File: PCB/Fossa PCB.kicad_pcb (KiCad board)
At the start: 2 copper layers, 115.6 x 77.5 mm, 17 parts, among them J1 WT32-SC01, J2 NV10 USB+, J3 DG600F, J4 Barrel_Jack_MountingPin

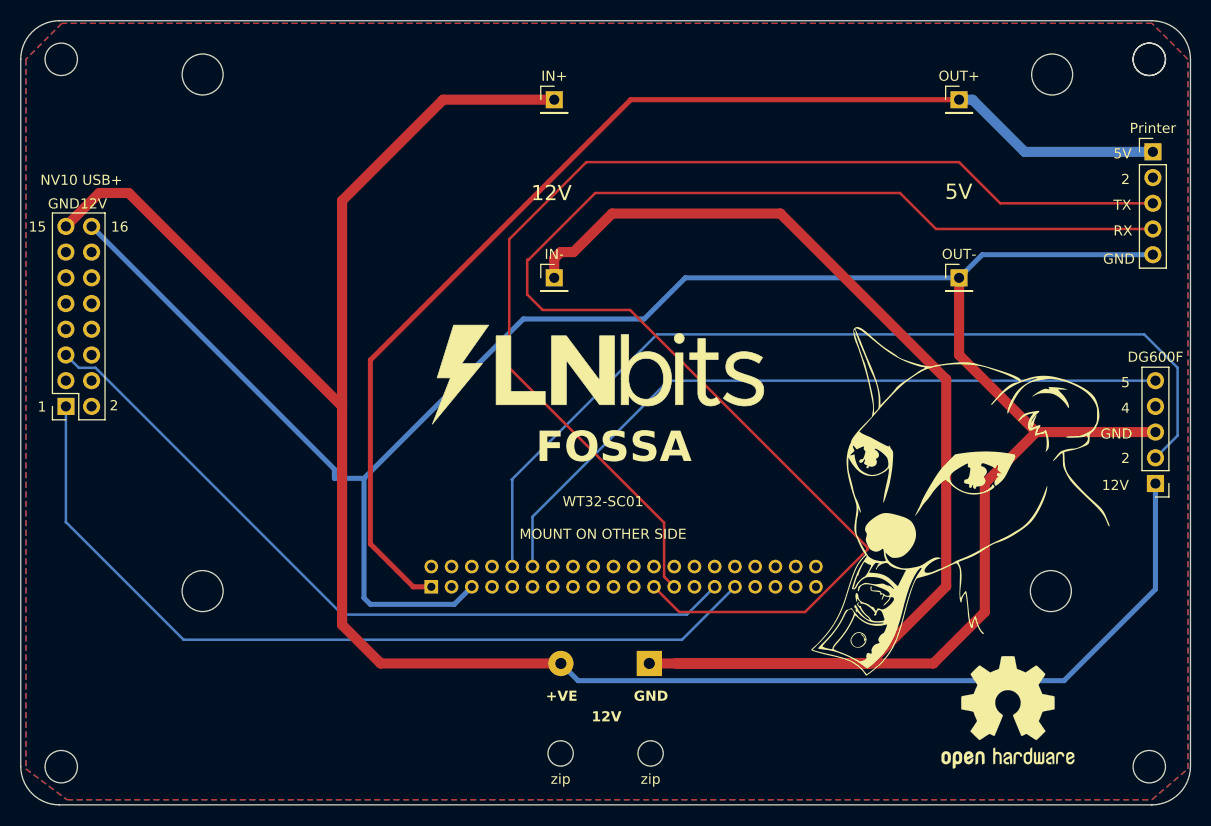
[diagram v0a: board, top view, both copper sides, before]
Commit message: Added Wiring diagram and organised docs a bit
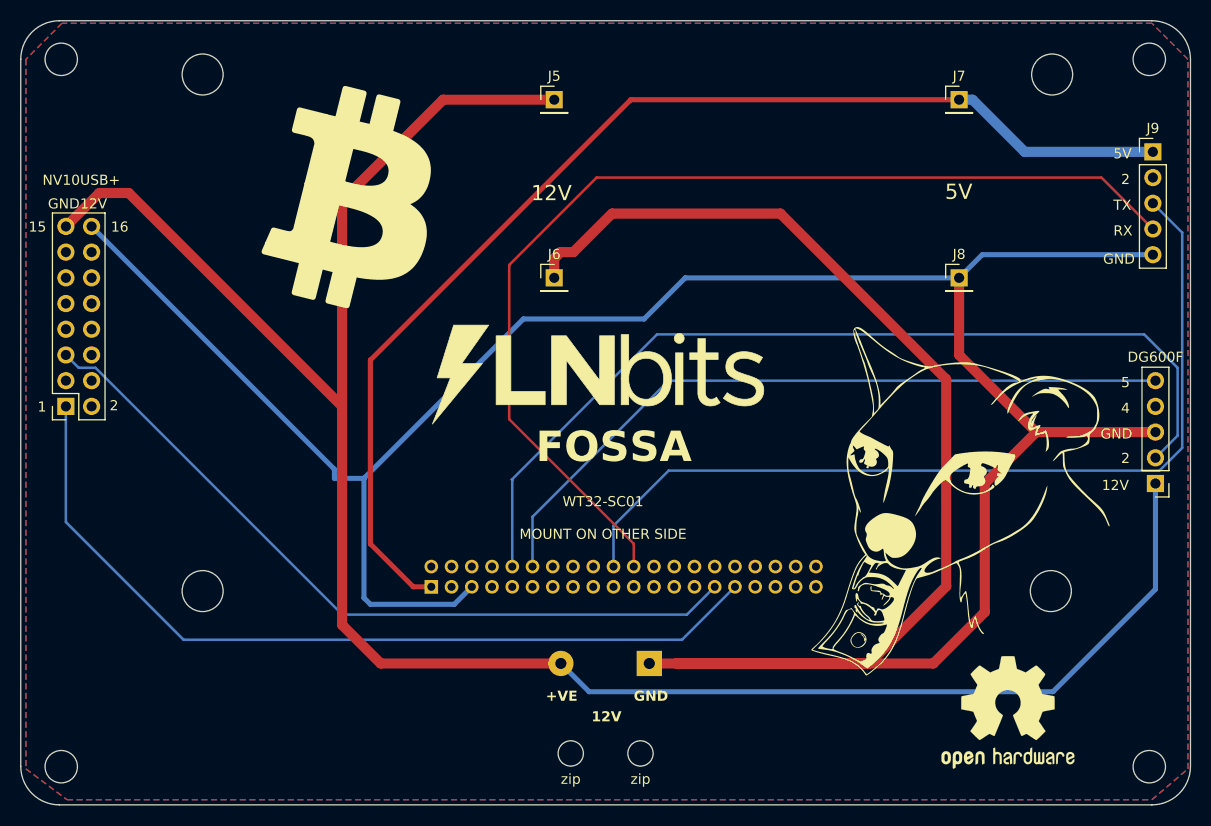
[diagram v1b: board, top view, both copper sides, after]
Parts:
- removed ?: , 
- J2: value NV10 USB+ -> NV10USB+
- J9: renamed from Printer; value J9 -> Printer
- moved zip 1.00 mm to (140.7, 149.9)
- moved zip 1.00 mm to (147.6, 149.9)
- renumbered IN+ to J5, IN- to J6, OUT+ to J7, OUT- to J8
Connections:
- J1 pad 20: unconnected-(J1-Pin_20-Pad20) -> Net-(J1-Pin_20)
- J1 pad 22: unconnected-(J1-Pin_22-Pad22) -> Net-(J1-Pin_22)
- J1 pad 23: Net-(J1-Pin_23) -> unconnected-(J1-Pin_23-Pad23)
- J1 pad 25: Net-(J1-Pin_25) -> unconnected-(J1-Pin_25-Pad25)
- J3 pad 3: Net-(J1-Pin_5) -> Net-(J2-Pin_15)
- J4 pad 1: Net-(J1-Pin_5) -> Net-(J6-Pin_1)
- J6 pad 1: Net-(J1-Pin_5) -> Net-(J6-Pin_1)
- J9 pad 3: Net-(J1-Pin_25) -> Net-(J1-Pin_20)
- J9 pad 4: Net-(J1-Pin_23) -> Net-(J1-Pin_22)
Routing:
- net Net-(J1-Pin_23): track 138.3 -> 0.00 mm
- net Net-(J1-Pin_25): track 109.5 -> 0.00 mm
- net Net-(J1-Pin_22): track 0.00 -> 104.2 mm
- net Net-(J1-Pin_20): track 0.00 -> 88.8 mm
- net Net-(J2-Pin_15): track 201.2 -> 202.1 mm
